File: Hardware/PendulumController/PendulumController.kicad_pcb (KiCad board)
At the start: 2 copper layers, 157 x 47 mm, 79 parts, among them J101 MOTOR, J102 ENCODER, J201 ICSP, J202 Limit, J302 19V Input, J401 USBC, J402 PROG, Q101 MMBT3904, Q102 MMBT3906, SW201 RESET, SW202 START_SW, SW203 STOP/MODE_SW, U201 ATmega328P, U301 NCV1117ST50T3G, U401 FT232RL, Y201 16mHz

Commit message: NOW its perfect
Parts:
- added G***: LOGO, Misc:guo, B.Cu at (190.5, 75.0)

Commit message: Last cleanups!
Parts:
- removed R103: TBD, Resistor_SMD:R_0805_2012Metric
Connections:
- A101 pad 14: /EN -> Net-(A101-Pad14)
- A101 pad 9: unconnected-(A101-Pad9) -> /EN
- JP101 pad 2: /EN -> Net-(A101-Pad14)
- Q102 pad 3: Net-(Q102-Pad3) -> /TFT_LED
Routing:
- net /EN: track 73.7 -> 83.3 mm
- net /TFT_LED: track 17.9 -> 22.0 mm
- net Net-(A101-Pad14): track 0.00 -> 3.70 mm
- net Net-(Q102-Pad3): track 2.60 -> 0.00 mm
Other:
- board text added: "Kat wuz here"

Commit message: Tidy brd
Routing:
- net /MCU/AnalogP: track 65.0 -> 64.3 mm
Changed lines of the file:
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@@
     (pad "6" thru_hole oval (at 0 12.7 90) (size 1.7 1.7) (drill 1) (layers *.Cu *.Mask)
       (net 1 "GND") (pinfunction "Pin_6") (pintype "passive"))
-    (model "${KICAD6_3DMODEL_DIR}/Connector_PinSocket_2.54mm.3dshapes/PinSocket_1x06_P2.54mm_Vertical.wrl"
+    (model "${KICAD6_3DMODEL_DIR}/Connector_PinSocket_2.54mm.3dshapes/PinSocket_1x06_P2.54mm_Vertical.wrl" hide
       (offset (xyz 0 0 0))
       (scale (xyz 1 1 1))
@@
   (segment (start 147.75 84.75) (end 146.916726 84.75) (width 0.25) (layer "B.Cu") (net 63))
   (segment (start 145 75) (end 153.9375 75) (width 0.25) (layer "B.Cu") (net 63))
-  (segment (start 138.151903 79.55) (end 139.140775 78.561128) (width 0.25) (layer "F.Cu") (net 64))
-  (segment (start 127.669503 80.330497) (end 126.669503 80.330497) (width 0.25) (layer "F.Cu") (net 64))
-  (segment (start 130.186396 79.55) (end 138.151903 79.55) (width 0.25) (layer "F.Cu") (net 64))
-  (segment (start 130.186396 79.55) (end 129.318198 78.681802) (width 0.25) (layer "F.Cu") (net 64))
+  (segment (start 142.889555 78.561128) (end 139.140775 78.561128) (width 0.25) (layer "F.Cu") (net 64))
+  (segment (start 126.712701 80.287299) (end 126.669503 80.330497) (width 0.25) (layer "F.Cu") (net 64))
+  (segment (start 139.140775 78.561128) (end 138.151903 79.55) (width 0.25) (layer "F.Cu") (net 64))
   (segment (start 95 73) (end 90 73) (width 0.25) (layer "F.Cu") (net 64))
+  (segment (start 143.40901 79.080583) (end 142.889555 78.561128) (width 0.25) (layer "F.Cu") (net 64))
+  (segment (start 129.788299 79.55) (end 129.051 80.287299) (width 0.25) (layer "F.Cu") (net 64))
   (segment (start 97 75) (end 95 73) (width 0.25) (layer "F.Cu") (net 64))
-  (segment (start 139.140775 78.561128) (end 142.889555 78.561128) (width 0.25) (layer "F.Cu") (net 64))
+  (segment (start 138.151903 79.55) (end 129.788299 79.55) (width 0.25) (layer "F.Cu") (net 64))
   (segment (start 90 73) (end 86.5 69.5) (width 0.25) (layer "F.Cu") (net 64))
-  (segment (start 143.40901 79.080583) (end 142.889555 78.561128) (width 0.25) (layer "F.Cu") (net 64))
-  (segment (start 129.318198 78.681802) (end 127.669503 80.330497) (width 0.25) (layer "F.Cu") (net 64))
+  (segment (start 129.051 80.287299) (end 126.712701 80.287299) (width 0.25) (layer "F.Cu") (net 64))
   (via (at 126.669503 80.330497) (size 0.8) (drill 0.4) (layers "F.Cu" "B.Cu") (net 64))
   (via (at 97 75) (size 0.8) (drill 0.4) (layers "F.Cu" "B.Cu") (net 64))

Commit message: Weird debugging issue
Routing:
- net +5V: track 330.0 -> 330.6 mm
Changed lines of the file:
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@@
   (segment (start 150.078249 79.078249) (end 149.987437 79.078249) (width 0.25) (layer "F.Cu") (net 2))
   (segment (start 161.155 84.75) (end 162.75 84.75) (width 0.25) (layer "F.Cu") (net 3))
-  (segment (start 148.749963 82.578464) (end 148.421536 82.578464) (width 0.55) (layer "F.Cu") (net 3))
   (segment (start 119.75 73.85) (end 119.75 75.25) (width 0.25) (layer "F.Cu") (net 3))
   (segment (start 135 110.5) (end 135 108.5) (width 0.25) (layer "F.Cu") (net 3))
@@
   (segment (start 199.725 83.6) (end 199.725 85.675) (width 0.45) (layer "F.Cu") (net 3))
   (segment (start 202.975 76.4) (end 202.975 78.525) (width 0.45) (layer "F.Cu") (net 3))
-  (segment (start 149.419417 81.90901) (end 148.749963 82.578464) (width 0.55) (layer "F.Cu") (net 3))
   (segment (start 141.523187 88.023187) (end 141.5 88) (width 0.55) (layer "F.Cu") (net 3))
   (segment (start 162 108.5) (end 162 97.75) (width 0.25) (layer "F.Cu") (net 3))
@@
   (segment (start 141.777639 86.222361) (end 143 85) (width 0.55) (layer "F.Cu") (net 3))
   (segment (start 202.5 89.5) (end 199.8 86.8) (width 1) (layer "F.Cu") (net 3))
+  (segment (start 149.419417 81.90901) (end 148.328427 83) (width 0.55) (layer "F.Cu") (net 3))
   (segment (start 119.75 75.25) (end 119.5 75.5) (width 0.25) (layer "F.Cu") (net 3))
   (segment (start 203.55 93.45) (end 204.1 94) (width 1) (layer "F.Cu") (net 3))
@@
   (segment (start 141.5 88) (end 141.343502 88) (width 0.55) (layer "F.Cu") (net 3))
   (segment (start 142.843324 87.353732) (end 142.173869 88.023187) (width 0.55) (layer "F.Cu") (net 3))
+  (segment (start 148.328427 83) (end 148 83) (width 0.55) (layer "F.Cu") (net 3))
   (segment (start 188.5 69.3125) (end 189.3125 69.3125) (width 1) (layer "F.Cu") (net 3))
   (segment (start 200.45 93.45) (end 201.95 93.45) (width 1) (layer "F.Cu") (net 3))

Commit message: Configure for usbasp
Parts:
- added R103: 50R, Resistor_SMD:R_0805_2012Metric, F.Cu at (115.5, 81.6)
- added R104: 50R, Resistor_SMD:R_0805_2012Metric, F.Cu at (119.5, 81.6)
- added R105: 50R, Resistor_SMD:R_0805_2012Metric, F.Cu at (117.5, 78.0)
- C201, C202: value 100nf -> 100nF
- moved TP103 7.81 mm to (115.5, 85.0)
- moved TP106 7.43 mm to (126.0, 90.0)
- moved TP104 5.00 mm to (117.5, 85.0)
- moved TP105 2.24 mm to (119.5, 85.0)
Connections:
- C102 pad 13: /SDO -> Net-(C102-Pad13)
- C102 pad 14: /SDI -> Net-(C102-Pad14)
- C102 pad 15: /SCK -> Net-(C102-Pad15)
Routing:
- net Net-(C102-Pad15): track 0.00 -> 11.3 mm
- net /SDO: track 76.3 -> 65.3 mm
- net /SCK: track 81.5 -> 71.9 mm
- net Net-(C102-Pad13): track 0.00 -> 7.96 mm
- net /SDI: track 74.2 -> 67.5 mm
- net Net-(C102-Pad14): track 0.00 -> 6.43 mm
- net +5V: track 330.6 -> 334.2 mm
- net /DATA/COMMAND: track 53.1 -> 54.2 mm
- net GND: vias 33 -> 34

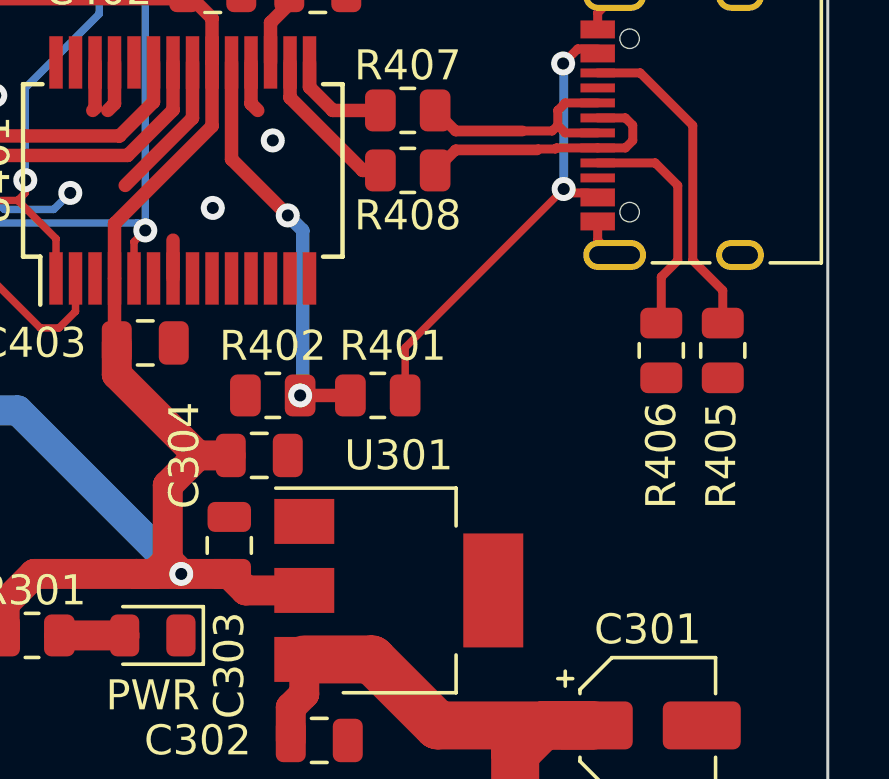
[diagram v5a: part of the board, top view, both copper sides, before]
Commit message: include vbus bypass diode
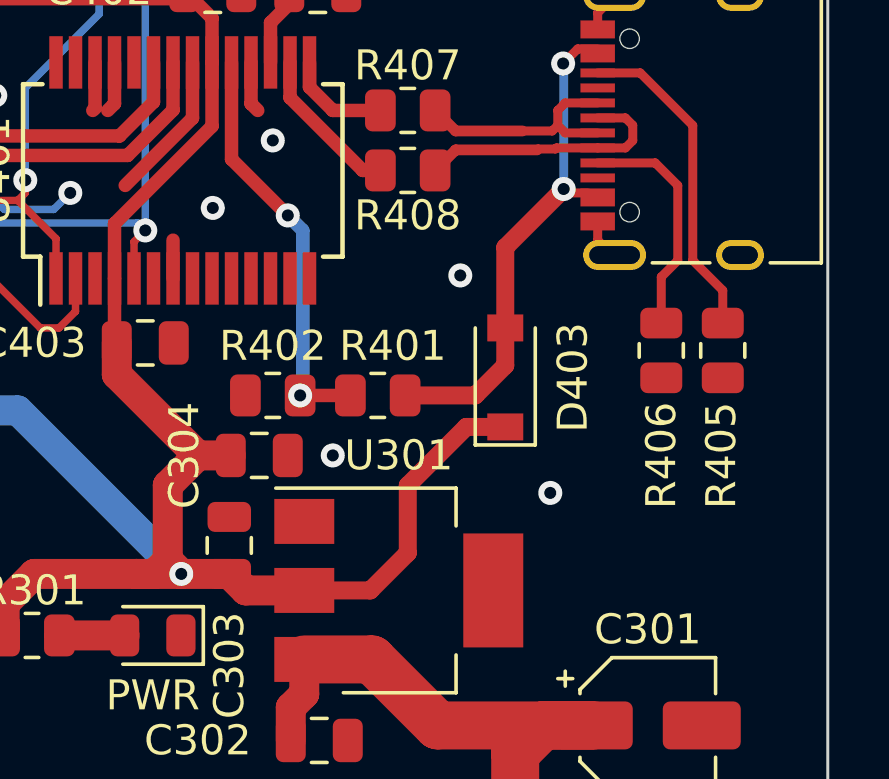
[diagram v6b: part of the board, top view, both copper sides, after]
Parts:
- added D403: MBR0520, Diode_SMD:D_SOD-123, F.Cu at (212.8, 86.9)
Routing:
- net +5V: track 334.2 -> 344.4 mm
- net VBUS: track 15.4 -> 16.8 mm
- net GND: vias 34 -> 37
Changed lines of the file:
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@@
       (net 30 "Net-(A101-Pad14)") (pinfunction "B") (pintype "passive"))
   )
+  (footprint "Diode_SMD:D_SOD-123" (layer "F.Cu")
+    (at 212.75 86.9 90)
+    (descr "SOD-123")
+    (tags "SOD-123")
+    (property "Sheetfile" "prog.kicad_sch")
+    (property "Sheetname" "Programming")
+    (attr smd)
+    (fp_text reference "D403" (at 0 2.25 90) (layer "F.SilkS")
+      (effects (font (size 1 1) (thickness 0.15)))
+    )
+    (fp_text value "MBR0520" (at 0 0 90) (layer "F.Fab")
+      (effects (font (size 1 1) (thickness 0.15)))
+    )
+    (fp_text user "${REFERENCE}" (at 0 0 90) (layer "F.Fab")
+      (effects (font (size 1 1) (thickness 0.15)))
+    )
+    (fp_line (start -2.25 -1) (end -2.25 1) (layer "F.SilkS") (width 0.12))
+    (fp_line (start -2.25 -1) (end 1.65 -1) (layer "F.SilkS") (width 0.12))
+    (fp_line (start -2.25 1) (end 1.65 1) (layer "F.SilkS") (width 0.12))
+    (fp_line (start 2.35 -1.15) (end 2.35 1.15) (layer "F.CrtYd") (width 0.05))
+    (fp_line (start -2.35 -1.15) (end 2.35 -1.15) (layer "F.CrtYd") (width 0.05))
+    (fp_line (start 2.35 1.15) (end -2.35 1.15) (layer "F.CrtYd") (width 0.05))
+    (fp_line (start -2.35 -1.15) (end -2.35 1.15) (layer "F.CrtYd") (width 0.05))
+    (fp_line (start 0.25 0) (end 0.75 0) (layer "F.Fab") (width 0.1))
+    (fp_line (start -0.35 0) (end 0.25 -0.4) (layer "F.Fab") (width 0.1))
+    (fp_line (start -0.35 0) (end -0.35 0.55) (layer "F.Fab") (width 0.1))
+    (fp_line (start 1.4 -0.9) (end 1.4 0.9) (layer "F.Fab") (width 0.1))
+    (fp_line (start -0.75 0) (end -0.35 0) (layer "F.Fab") (width 0.1))
+    (fp_line (start 1.4 0.9) (end -1.4 0.9) (layer "F.Fab") (width 0.1))
+    (fp_line (start -0.35 0) (end -0.35 -0.55) (layer "F.Fab") (width 0.1))
+    (fp_line (start -1.4 0.9) (end -1.4 -0.9) (layer "F.Fab") (width 0.1))
+    (fp_line (start 0.25 -0.4) (end 0.25 0.4) (layer "F.Fab") (width 0.1))
+    (fp_line (start 0.25 0.4) (end -0.35 0) (layer "F.Fab") (width 0.1))
+    (fp_line (start -1.4 -0.9) (end 1.4 -0.9) (layer "F.Fab") (width 0.1))
+    (pad "1" smd rect (at -1.65 0 90) (size 0.9 1.2) (layers "F.Cu" "F.Paste" "F.Mask")
+      (net 3 "+5V") (pinfunction "K") (pintype "passive"))
+    (pad "2" smd rect (at 1.65 0 90) (size 0.9 1.2) (layers "F.Cu" "F.Paste" "F.Mask")
+      (net 41 "VBUS") (pinfunction "A") (pintype "passive"))
+    (model "${KICAD6_3DMODEL_DIR}/Diode_SMD.3dshapes/D_SOD-123.wrl"
+      (offset (xyz 0 0 0))
+      (scale (xyz 1 1 1))
+      (rotate (xyz 0 0 0))
+    )
+  )
   (footprint "Resistor_SMD:R_0805_2012Metric" (layer "F.Cu")
     (at 160 97 90)
@@
   (via (at 138.5 81.5) (size 0.8) (drill 0.4) (layers "F.Cu" "B.Cu") (free) (net 1))
   (via (at 141.75 72.5125) (size 0.8) (drill 0.4) (layers "F.Cu" "B.Cu") (free) (net 1))
+  (via (at 207 89.5) (size 0.8) (drill 0.4) (layers "F.Cu" "B.Cu") (free) (net 1))
   (via (at 129 95) (size 0.8) (drill 0.4) (layers "F.Cu" "B.Cu") (free) (net 1))
   (via (at 154.25 82) (size 0.8) (drill 0.4) (layers "F.Cu" "B.Cu") (free) (net 1))
+  (via (at 214.25 90.75) (size 0.8) (drill 0.4) (layers "F.Cu" "B.Cu") (free) (net 1))
   (via (at 145 77.25) (size 0.8) (drill 0.4) (layers "F.Cu" "B.Cu") (free) (net 1))
   (via (at 139 89) (size 0.8) (drill 0.4) (layers "F.Cu" "B.Cu") (free) (net 1))
@@
   (via (at 154 93) (size 0.8) (drill 0.4) (layers "F.Cu" "B.Cu") (free) (net 1))
   (via (at 205 79) (size 0.8) (drill 0.4) (layers "F.Cu" "B.Cu") (free) (net 1))
+  (via (at 211.25 83.5) (size 0.8) (drill 0.4) (layers "F.Cu" "B.Cu") (free) (net 1))
   (via (at 164.5 83) (size 0.8) (drill 0.4) (layers "F.Cu" "B.Cu") (free) (net 1))
   (via (at 195.75 77.5) (size 0.8) (drill 0.4) (layers "F.Cu" "B.Cu") (free) (net 1))
@@
   (segment (start 149.987437 79.078249) (end 148.288047 80.777639) (width 0.25) (layer "F.Cu") (net 2))
   (segment (start 150.078249 79.078249) (end 149.987437 79.078249) (width 0.25) (layer "F.Cu") (net 2))
+  (segment (start 211.45 88.55) (end 209.5 90.5) (width 0.6) (layer "F.Cu") (net 3))
   (segment (start 161.155 84.75) (end 162.75 84.75) (width 0.25) (layer "F.Cu") (net 3))
   (segment (start 135 110.5) (end 135 108.5) (width 0.25) (layer "F.Cu") (net 3))
@@
   (segment (start 199.725 83.6) (end 199.725 85.675) (width 0.45) (layer "F.Cu") (net 3))
   (segment (start 202.975 76.4) (end 202.975 78.525) (width 0.45) (layer "F.Cu") (net 3))
+  (segment (start 212.75 88.55) (end 211.45 88.55) (width 0.6) (layer "F.Cu") (net 3))
   (segment (start 118 75) (end 119.5 75) (width 0.25) (layer "F.Cu") (net 3))
   (segment (start 141.523187 88.023187) (end 141.5 88) (width 0.55) (layer "F.Cu") (net 3))
@@
   (segment (start 141.343502 88) (end 140.671751 88.671751) (width 0.55) (layer "F.Cu") (net 3))
   (segment (start 141.711953 86.222361) (end 141.777639 86.222361) (width 0.55) (layer "F.Cu") (net 3))
+  (segment (start 209.5 92.75) (end 208.25 94) (width 0.6) (layer "F.Cu") (net 3))
   (segment (start 199.725 81.775) (end 199.725 83.6) (width 0.45) (layer "F.Cu") (net 3))
   (segment (start 160 97.9125) (end 161.3375 97.9125) (width 0.25) (layer "F.Cu") (net 3))
   (segment (start 136.45 71.3) (end 136.45 73.45) (width 0.6) (layer "F.Cu") (net 3))
   (segment (start 160.135 85.77) (end 161.155 84.75) (width 0.25) (layer "F.Cu") (net 3))
+  (segment (start 209.5 90.5) (end 209.5 92.75) (width 0.6) (layer "F.Cu") (net 3))
   (segment (start 197.05 93.45) (end 200.45 93.45) (width 1) (layer "F.Cu") (net 3))
   (segment (start 141.777639 86.222361) (end 143 85) (width 0.55) (layer "F.Cu") (net 3))
   (segment (start 202.5 89.5) (end 199.8 86.8) (width 1) (layer "F.Cu") (net 3))
   (segment (start 149.419417 81.90901) (end 148.328427 83) (width 0.55) (layer "F.Cu") (net 3))
+  (segment (start 208.25 94) (end 206.05 94) (width 0.6) (layer "F.Cu") (net 3))
   (segment (start 203.55 93.45) (end 204.1 94) (width 1) (layer "F.Cu") (net 3))
   (segment (start 202.5 89.5) (end 203.6 89.5) (width 1) (layer "F.Cu") (net 3))
@@
   (segment (start 188.5 72.8375) (end 188.5 71.1875) (width 1) (layer "F.Cu") (net 39))
   (segment (start 186 72.8375) (end 186 71.1875) (width 1) (layer "F.Cu") (net 40))
-  (segment (start 209.4125 85.903251) (end 214.69688 80.618871) (width 0.25) (layer "F.Cu") (net 41))
   (segment (start 214.69688 80.618871) (end 214.828009 80.75) (width 0.3) (layer "F.Cu") (net 41))
+  (segment (start 212.75 85.25) (end 212.75 86.5) (width 0.6) (layer "F.Cu") (net 41))
   (segment (start 214.828009 80.75) (end 215.5 80.75) (width 0.3) (layer "F.Cu") (net 41))
-  (segment (start 209.4125 87.5) (end 209.4125 85.903251) (width 0.25) (layer "F.Cu") (net 41))
+  (segment (start 212.75 86.5) (end 211.75 87.5) (width 0.6) (layer "F.Cu") (net 41))
   (segment (start 215.163869 75.95) (end 214.678565 76.435304) (width 0.3) (layer "F.Cu") (net 41))
+  (segment (start 211.75 87.5) (end 209.4125 87.5) (width 0.6) (layer "F.Cu") (net 41))
   (segment (start 215.83 75.95) (end 215.163869 75.95) (width 0.3) (layer "F.Cu") (net 41))
+  (segment (start 212.75 85.25) (end 212.75 82.565751) (width 0.6) (layer "F.Cu") (net 41))
+  (segment (start 212.75 82.565751) (end 214.69688 80.618871) (width 0.6) (layer "F.Cu") (net 41))
   (via (at 214.678565 76.435304) (size 0.8) (drill 0.4) (layers "F.Cu" "B.Cu") (net 41))
   (via (at 214.69688 80.618871) (size 0.8) (drill 0.4) (layers "F.Cu" "B.Cu") (net 41))

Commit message: More cleaning
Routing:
- net /EN: track 83.3 -> 81.8 mm
- net GND: vias 37 -> 38

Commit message: Revision 2 board
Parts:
- moved TP104 52.0 mm to (169.5, 82.8)
- moved R103 52.0 mm to (167.5, 82.0)
- moved R104 52.0 mm to (171.5, 82.0)
- moved R105 52.0 mm to (169.5, 78.5)
- moved TP103 52.0 mm to (167.5, 84.8)
- moved TP105 52.0 mm to (171.5, 84.8)
- moved TP108 50.1 mm to (177.0, 82.8)
- moved TP107 49.4 mm to (175.2, 84.8)
- moved C102 48.3 mm to (172.2, 72.0)
- moved TP106 48.1 mm to (173.5, 82.8)
- moved R201 16.1 mm to (182.2, 83.2)
- moved R202 16.1 mm to (182.2, 85.2)
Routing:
- net /SDI: track 67.5 -> 14.5 mm, vias 0 -> 1
- net /SCK: track 71.9 -> 22.7 mm
- net Net-(C404-Pad2): track 39.0 -> 0.00 mm
- net /SDO: track 65.3 -> 27.7 mm
- net /SD_CS: track 46.8 -> 22.6 mm, vias 2 -> 1
- net /MCU/RST: track 63.3 -> 39.9 mm
- net /TFT_LED: track 22.0 -> 0.00 mm
- net /RESET: track 33.0 -> 12.5 mm, vias 2 -> 0
- net /DATA/COMMAND: track 54.2 -> 34.6 mm, vias 2 -> 1
- net Net-(R202-Pad1): track 31.6 -> 13.8 mm, vias 2 -> 1
- net /TFT_CS: track 49.5 -> 32.3 mm, vias 2 -> 1
- net Net-(R201-Pad1): track 30.3 -> 13.5 mm, vias 2 -> 1
- net /MCU/RXD: track 44.0 -> 28.9 mm
- net /MCU/TXD: track 46.8 -> 32.3 mm
- net +5V: track 344.0 -> 337.7 mm, vias 6 -> 5
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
